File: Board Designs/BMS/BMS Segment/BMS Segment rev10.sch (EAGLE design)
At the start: 113 parts

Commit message: BMS segment rev10: silkscreen adjustments
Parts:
- C6_A, C6_B, C7_A, C7_B: value 0.1uF -> 100nF
- J: value Jumper -> 0R; TYPE (none) -> JUMPER
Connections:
- net V-_A: now also THERM3.1, THERM4.1; no longer THERM1.1, THERM2.1
- net V-_B: now also THERM1.1, THERM2.1; no longer THERM3.1, THERM4.1
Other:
- moved on the sheet: THERM1, THERM2, THERM3, THERM4
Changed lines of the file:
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@@
 <part name="U$2" library="HyTechDevices" deviceset="LTC6804-2" device=""/>
 <part name="C4_B" library="HyTechDevices" deviceset="CAP" device="0805" value="10nF"/>
-<part name="C6_B" library="HyTechDevices" deviceset="CAP" device="0805" value="0.1uF">
+<part name="C6_B" library="HyTechDevices" deviceset="CAP" device="0805" value="100nF">
 <attribute name="VOLTAGE" value="100V"/>
 </part>
@@
 <part name="SUPPLY9" library="supply2" deviceset="V-" device=""/>
 <part name="ISOSPI_B" library="HyTechDevices" deviceset="CONNECTOR-2" device="NANO-FIT_VERTICAL-2"/>
-<part name="THERM3" library="HyTechDevices" deviceset="THERMISTOR_NCP21" device="0603" value="10K"/>
-<part name="THERM4" library="HyTechDevices" deviceset="THERMISTOR_NCP21" device="0603" value="10K"/>
+<part name="THERM2" library="HyTechDevices" deviceset="THERMISTOR_NCP21" device="0603" value="10K"/>
+<part name="THERM1" library="HyTechDevices" deviceset="THERMISTOR_NCP21" device="0603" value="10K"/>
 <part name="SUPPLY10" library="supply2" deviceset="V-" device=""/>
 <part name="SUPPLY11" library="supply2" deviceset="V-" device=""/>
@@
 <part name="U$1" library="HyTechDevices" deviceset="LTC6804-2" device=""/>
 <part name="C4_A" library="HyTechDevices" deviceset="CAP" device="0805" value="10nF"/>
-<part name="C6_A" library="HyTechDevices" deviceset="CAP" device="0805" value="0.1uF">
+<part name="C6_A" library="HyTechDevices" deviceset="CAP" device="0805" value="100nF">
 <attribute name="VOLTAGE" value="100V"/>
 </part>
@@
 <part name="AMS_TEST_PORT1" library="HyTechDevices" deviceset="CONNECTOR-2" device="NANO-FIT_VERTICAL-2" value="CONNECTOR-2NANO-FIT_VERTICAL-2"/>
 <part name="ISOSPI_A" library="HyTechDevices" deviceset="CONNECTOR-2" device="NANO-FIT_VERTICAL-2"/>
-<part name="THERM1" library="HyTechDevices" deviceset="THERMISTOR_NCP21" device="0603" value="10K"/>
-<part name="THERM2" library="HyTechDevices" deviceset="THERMISTOR_NCP21" device="0603" value="10K"/>
+<part name="THERM4" library="HyTechDevices" deviceset="THERMISTOR_NCP21" device="0603" value="10K"/>
+<part name="THERM3" library="HyTechDevices" deviceset="THERMISTOR_NCP21" device="0603" value="10K"/>
 <part name="SUPPLY37" library="supply1" deviceset="V-" device=""/>
 <part name="SUPPLY38" library="supply1" deviceset="V-" device=""/>
@@
 <part name="SUPPLY57" library="supply1" deviceset="V-" device=""/>
 <part name="SUPPLY58" library="supply1" deviceset="V-" device=""/>
-<part name="J" library="HyTechDevices" deviceset="RESISTOR" device="0805-RES" value="Jumper"/>
+<part name="J" library="HyTechDevices" deviceset="RESISTOR" device="0805-RES" value="0R">
+<attribute name="TYPE" value="JUMPER"/>
+</part>
 <part name="SUPPLY39" library="supply1" deviceset="V-" device=""/>
 <part name="SUPPLY59" library="supply2" deviceset="V-" device=""/>
@@
 <part name="THERM3_B" library="HyTechDevices" deviceset="CONNECTOR-2" device="NANO-FIT_VERTICAL-2" value="Th1"/>
 <part name="U$3" library="HyTechDevices" deviceset="NSV1C201MZ4" device=""/>
-<part name="C7_A" library="HyTechDevices" deviceset="CAP" device="0805" value="0.1uF">
+<part name="C7_A" library="HyTechDevices" deviceset="CAP" device="0805" value="100nF">
 <attribute name="VOLTAGE" value="100V"/>
 </part>
@@
 <part name="SUPPLY40" library="supply1" deviceset="V-" device=""/>
 <part name="U$4" library="HyTechDevices" deviceset="NSV1C201MZ4" device=""/>
-<part name="C7_B" library="HyTechDevices" deviceset="CAP" device="0805" value="0.1uF">
+<part name="C7_B" library="HyTechDevices" deviceset="CAP" device="0805" value="100nF">
 <attribute name="VOLTAGE" value="100V"/>
 </part>
@@
 <attribute name="VALUE" x="67.818" y="123.317" size="1.778" layer="96"/>
 </instance>
-<instance part="THERM3" gate="G$1" x="147.32" y="-2.54" smashed="yes">
+<instance part="THERM2" gate="G$1" x="147.32" y="-2.54" smashed="yes">
 <attribute name="NAME" x="143.002" y="0" size="1.778" layer="95"/>
 <attribute name="VALUE" x="144.78" y="-6.858" size="1.778" layer="96"/>
 </instance>
-<instance part="THERM4" gate="G$1" x="147.32" y="-22.86" smashed="yes">
+<instance part="THERM1" gate="G$1" x="147.32" y="-22.86" smashed="yes">
 <attribute name="NAME" x="143.002" y="-20.32" size="1.778" layer="95"/>
 <attribute name="VALUE" x="144.78" y="-27.178" size="1.778" layer="96"/>
@@
 <attribute name="VALUE" x="67.818" y="362.077" size="1.778" layer="96"/>
 </instance>
-<instance part="THERM1" gate="G$1" x="147.32" y="236.22" smashed="yes">
+<instance part="THERM4" gate="G$1" x="147.32" y="236.22" smashed="yes">
 <attribute name="NAME" x="143.002" y="238.76" size="1.778" layer="95"/>
 <attribute name="VALUE" x="144.78" y="231.902" size="1.778" layer="96"/>
 </instance>
-<instance part="THERM2" gate="G$1" x="147.32" y="215.9" smashed="yes">
+<instance part="THERM3" gate="G$1" x="147.32" y="215.9" smashed="yes">
 <attribute name="NAME" x="143.002" y="218.44" size="1.778" layer="95"/>
 <attribute name="VALUE" x="144.78" y="211.582" size="1.778" layer="96"/>
@@
 </instance>
 <instance part="J" gate="G$1" x="-172.72" y="276.86" smashed="yes">
-<attribute name="NAME" x="-176.53" y="278.3586" size="1.778" layer="95"/>
-<attribute name="VALUE" x="-173.99" y="273.558" size="1.778" layer="96"/>
+<attribute name="NAME" x="-178.53" y="274.3586" size="1.778" layer="95"/>
+<attribute name="VALUE" x="-172.99" y="274.558" size="1.778" layer="96"/>
+<attribute name="TYPE" x="-176.72" y="277.86" size="1.778" layer="96"/>
 </instance>
 <instance part="SUPPLY39" gate="1" x="-101.6" y="134.62" smashed="yes">
@@
 </segment>
 <segment>
-<pinref part="THERM3" gate="G$1" pin="1"/>
+<pinref part="THERM2" gate="G$1" pin="1"/>
 <pinref part="SUPPLY10" gate="1" pin="V-"/>
 <wire x1="152.4" y1="-2.54" x2="154.94" y2="-2.54" width="0.1524" layer="91"/>
 </segment>
 <segment>
-<pinref part="THERM4" gate="G$1" pin="1"/>
+<pinref part="THERM1" gate="G$1" pin="1"/>
 <pinref part="SUPPLY11" gate="1" pin="V-"/>
 <wire x1="152.4" y1="-22.86" x2="154.94" y2="-22.86" width="0.1524" layer="91"/>
@@
 <net name="N$19" class="0">
 <segment>
-<pinref part="THERM3" gate="G$1" pin="2"/>
+<pinref part="THERM2" gate="G$1" pin="2"/>
 <wire x1="142.24" y1="-2.54" x2="140.97" y2="-2.54" width="0.1524" layer="91"/>
 <portref moduleinst="THERM_FILTER4" port="THERM"/>
@@
 <segment>
 <portref moduleinst="THERM_FILTER5" port="THERM"/>
-<pinref part="THERM4" gate="G$1" pin="2"/>
+<pinref part="THERM1" gate="G$1" pin="2"/>
 <wire x1="142.24" y1="-22.86" x2="140.97" y2="-22.86" width="0.1524" layer="91"/>
 </segment>
@@
 <net name="N$34" class="0">
 <segment>
-<pinref part="THERM1" gate="G$1" pin="2"/>
+<pinref part="THERM4" gate="G$1" pin="2"/>
 <wire x1="142.24" y1="236.22" x2="140.97" y2="236.22" width="0.1524" layer="91"/>
 <portref moduleinst="THERM_FILTER9" port="THERM"/>
@@
 <segment>
 <portref moduleinst="THERM_FILTER10" port="THERM"/>
-<pinref part="THERM2" gate="G$1" pin="2"/>
+<pinref part="THERM3" gate="G$1" pin="2"/>
 <wire x1="142.24" y1="215.9" x2="140.97" y2="215.9" width="0.1524" layer="91"/>
 </segment>
@@
 </segment>
 <segment>
-<pinref part="THERM2" gate="G$1" pin="1"/>
+<pinref part="THERM3" gate="G$1" pin="1"/>
 <pinref part="SUPPLY38" gate="1" pin="V-"/>
 <wire x1="152.4" y1="215.9" x2="154.94" y2="215.9" width="0.1524" layer="91"/>
 </segment>
 <segment>
-<pinref part="THERM1" gate="G$1" pin="1"/>
+<pinref part="THERM4" gate="G$1" pin="1"/>
 <pinref part="SUPPLY37" gate="1" pin="V-"/>
 <wire x1="152.4" y1="236.22" x2="154.94" y2="236.22" width="0.1524" layer="91"/>

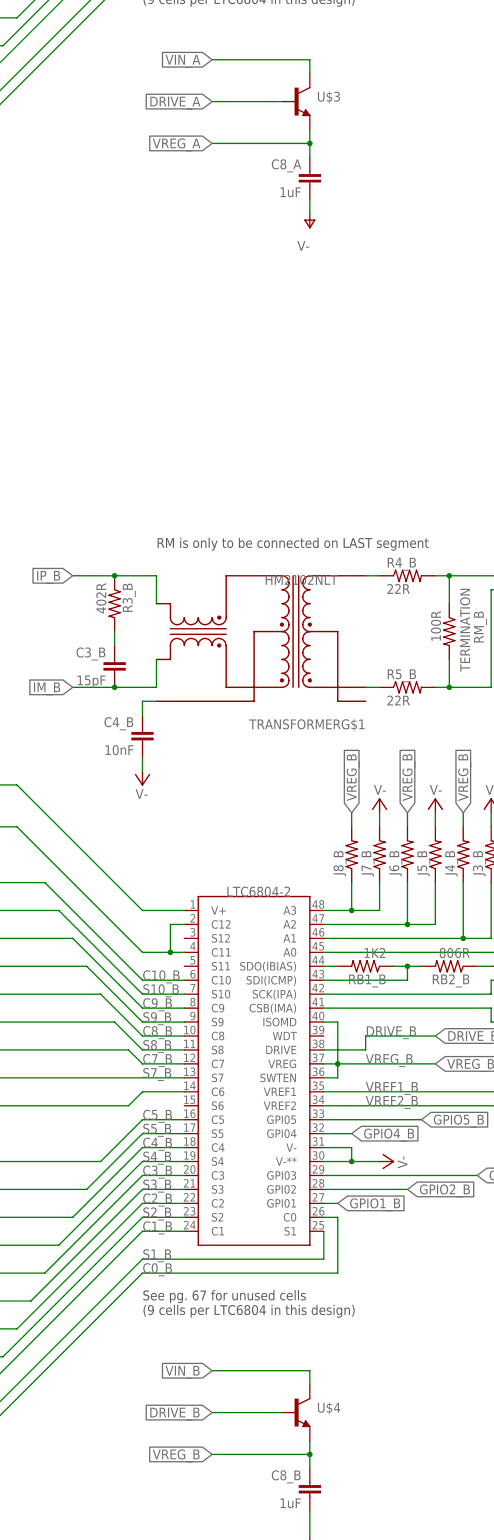
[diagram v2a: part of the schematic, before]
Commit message: BMS rev10: make # box bigger, added and moved test points
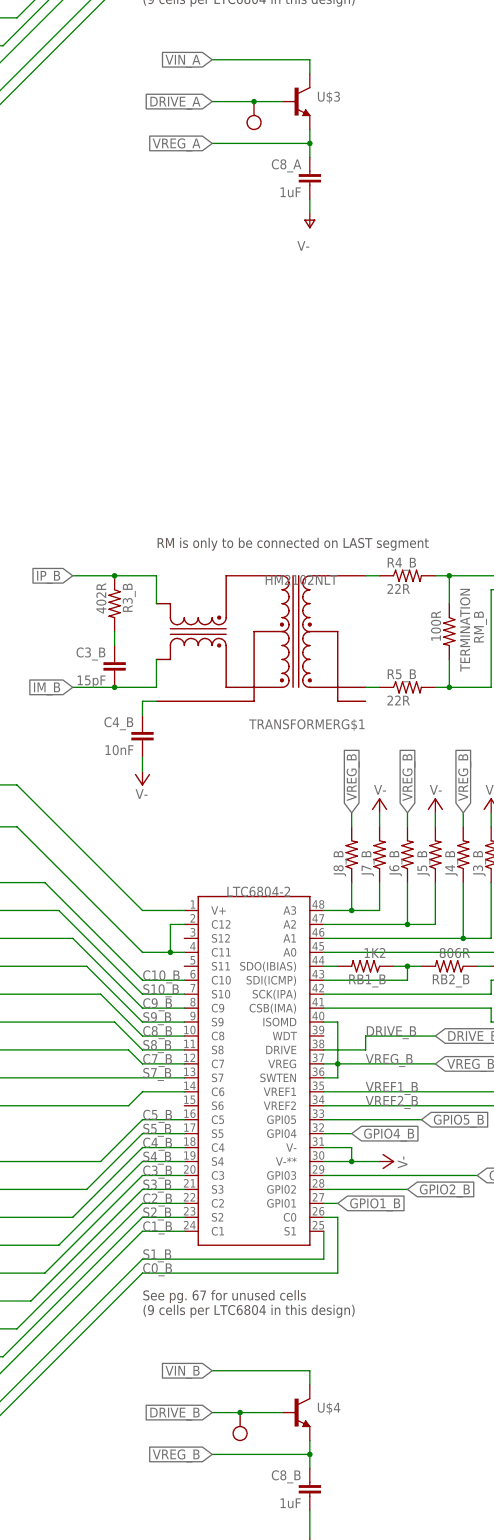
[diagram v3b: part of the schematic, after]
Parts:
- added U$7, U$8: TEST_POINT, HyTechDevices:TEST_POINT
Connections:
- net DRIVE_A: now also U$8.P$1
- net DRIVE_B: now also U$7.P$1
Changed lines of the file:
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@@
 <part name="U$5" library="HyTechDevices" deviceset="TEST_POINT" device=""/>
 <part name="U$6" library="HyTechDevices" deviceset="TEST_POINT" device=""/>
+<part name="U$7" library="HyTechDevices" deviceset="TEST_POINT" device=""/>
+<part name="U$8" library="HyTechDevices" deviceset="TEST_POINT" device=""/>
 </parts>
 <sheets>
@@
 <instance part="U$5" gate="G$1" x="-165.1" y="149.86" smashed="yes" rot="R180"/>
 <instance part="U$6" gate="G$1" x="-175.26" y="-88.9" smashed="yes" rot="R180"/>
+<instance part="U$7" gate="G$1" x="2.54" y="-33.02" smashed="yes" rot="R270"/>
+<instance part="U$8" gate="G$1" x="5.08" y="205.74" smashed="yes" rot="R270"/>
 </instances>
 <busses>
@@
 <segment>
 <pinref part="U$4" gate="G$1" pin="BASE"/>
-<wire x1="10.16" y1="-30.48" x2="-2.54" y2="-30.48" width="0.1524" layer="91"/>
+<wire x1="10.16" y1="-30.48" x2="2.54" y2="-30.48" width="0.1524" layer="91"/>
 <label x="-2.54" y="-30.48" size="1.778" layer="95" rot="R180" xref="yes"/>
+<pinref part="U$7" gate="G$1" pin="P$1"/>
+<wire x1="2.54" y1="-30.48" x2="-2.54" y2="-30.48" width="0.1524" layer="91"/>
+<junction x="2.54" y="-30.48"/>
 </segment>
 </net>
@@
 <segment>
 <pinref part="U$3" gate="G$1" pin="BASE"/>
-<wire x1="10.16" y1="208.28" x2="-2.54" y2="208.28" width="0.1524" layer="91"/>
+<wire x1="10.16" y1="208.28" x2="5.08" y2="208.28" width="0.1524" layer="91"/>
 <label x="-2.54" y="208.28" size="1.778" layer="95" rot="R180" xref="yes"/>
-</segment>
-</net>
+<pinref part="U$8" gate="G$1" pin="P$1"/>
+<wire x1="5.08" y1="208.28" x2="-2.54" y2="208.28" width="0.1524" layer="91"/>
+<junction x="5.08" y="208.28"/>
+</segment>
+</net>
